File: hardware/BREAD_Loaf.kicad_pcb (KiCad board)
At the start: 2 copper layers, 35.8 x 50.9 mm, 29 parts, among them J1 PPPC101LGBN-RC, J2 THING_PLUS_LOGICAL, Q1 BSS138, Q2 BSS138, Q3 BSS138, U1 AP63205WU-7, U2 LTC4311ISC6-TRMPBF

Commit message: fix(hw): re-point stale library nicknames
These parts exist in KiCad-Master-Lib; the boards referenced libraries that no
longer exist (kml-custom, KML-Custom, and SparkFun libraries that never
contained the part) or names the library has since changed.

KiCad embeds footprint geometry in the .kicad_pcb, so the boards rendered and
fabricated correctly and the rot stayed invisible -- it only surfaces on
update-from-library, or when a generator tries to resolve a nickname.

Nickname/name only. No geometry is changed:

  KML-Custom:Thermal Pad -> KMLib_Mounting:Thermal_Pad
  SparkFun-DiscreteSemi:AP63205 -> KMLib_IC_Power:AP63205WU-7_Buck_Regulator
  SparkFun-LED:WS2812-5050-4PIN -> KMLib_IC_SMD:WS2812-5050-4PIN

Only references that failed to resolve were touched. Generic parts (<=4 pins)
and KiCad *-rescue libraries are deliberately excluded: fingerprint matching
cannot distinguish a 2-pin resistor from a 2-pin capacitor, so those are being
done by hand.
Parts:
- D1: footprint SparkFun-LED:WS2812-5050-4PIN -> KMLib_IC_SMD:WS2812-5050-4PIN
- HS1: footprint KML-Custom:Thermal Pad -> KMLib_Mounting:Thermal_Pad
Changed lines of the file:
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@@
 		(embedded_fonts no)
 	)
-	(footprint "KML-Custom:Thermal Pad"
+	(footprint "KMLib_Mounting:Thermal_Pad"
 		(layer "F.Cu")
 		(at 64.55 112.35)
@@
 		(embedded_fonts no)
 	)
-	(footprint "SparkFun-LED:WS2812-5050-4PIN"
+	(footprint "KMLib_IC_SMD:WS2812-5050-4PIN"
 		(layer "F.Cu")
 		(at 64 121.05 180)

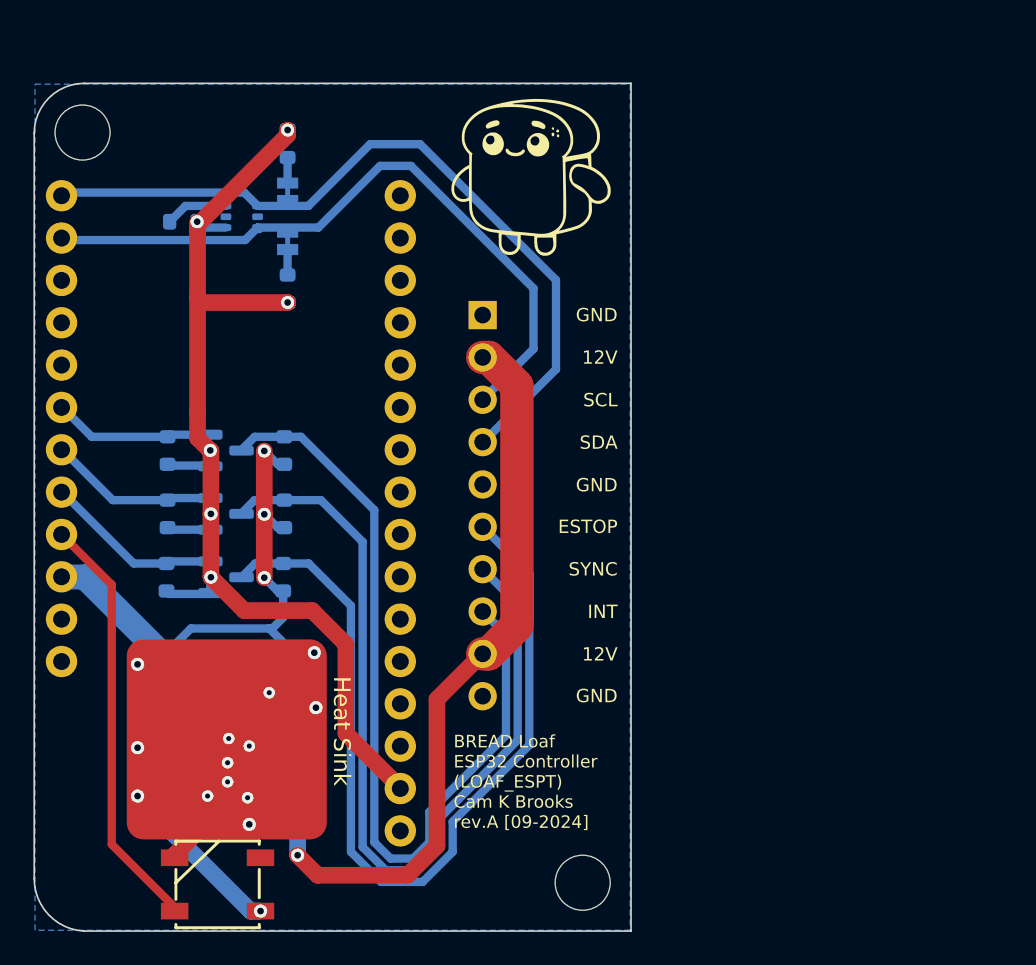
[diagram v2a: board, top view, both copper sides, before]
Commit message: fix(hw): re-point remaining library references
Every symbol now resolves against KiCad-Master-Lib:

  LTC4311:LTC4311ISC6-TRMPBF        -> KMLib_IC_Digital:LTC4311ISC6-TRMPBF
  SparkFun-RF:ESP_THING_PLUS_LOGICAL -> SparkFun-Board:ThingPlus_With_Connectors
  SparkFun-Hardware:Stand_off, PPPC101LGBN-RC, Arc  -> resolved

Board is clean: validate_board PASS, 0 ERC errors, 0 DRC errors.
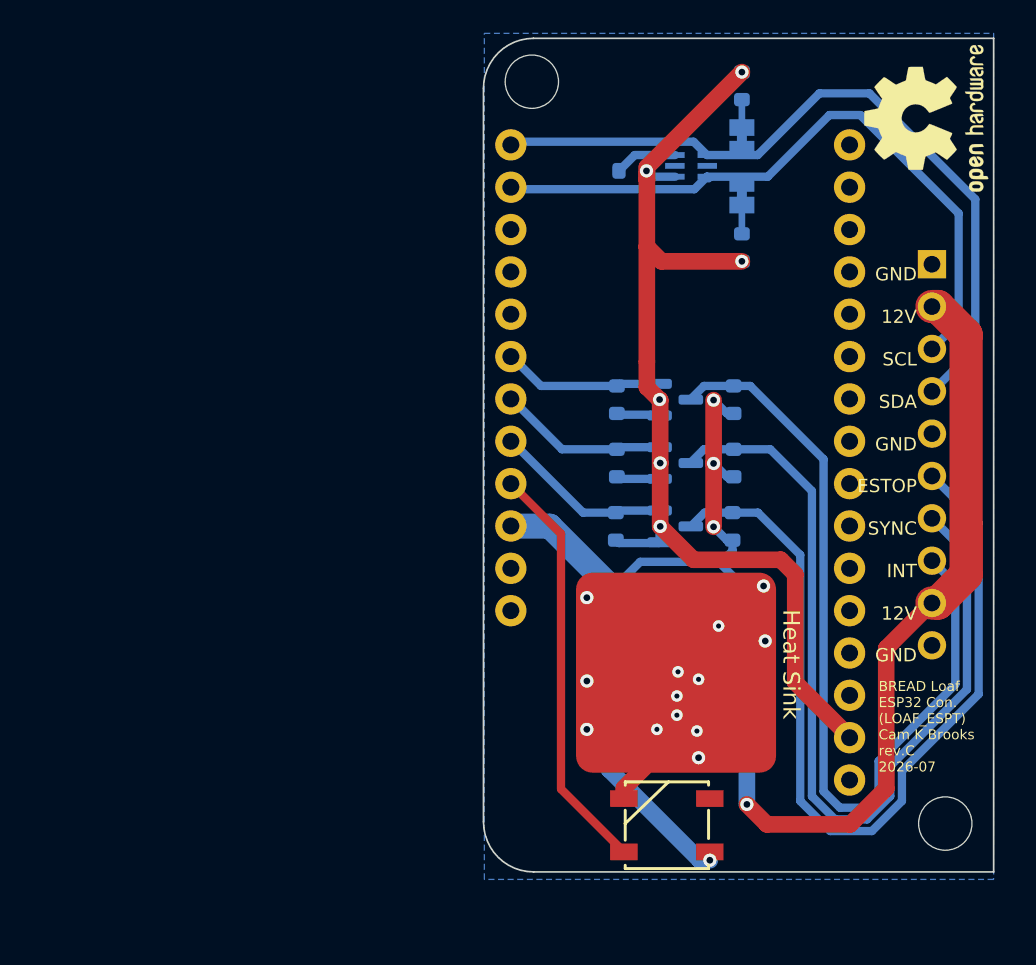
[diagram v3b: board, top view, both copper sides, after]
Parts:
- removed J1: PPPC101LGBN-RC, Connector_PinSocket_2.54mm:PinSocket_1x10_P2.54mm_Horizontal
- removed J2: THING_PLUS_LOGICAL, SparkFun-Board:ThingPlus
- removed JP1, JP2: ~, SparkFun-Jumper:Jumper_2_NC_Trace
- removed ST1, ST2: Stand_off, SparkFun-Hardware:Standoff
- removed demo**: Arc, Arc
- added H1: MountingHole, MountingHole:MountingHole_3.2mm_M3, F.Cu at (107.7, 117.4)
- added H2: MountingHole, MountingHole:MountingHole_3.2mm_M3, F.Cu at (82.8, 72.9)
- added J3: Conn_01x10_Socket, Connector_PinSocket_2.54mm:PinSocket_1x10_P2.54mm_Horizontal, B.Cu at (106.8, 83.8)
- added JP3: SolderJumper_2_Bridged, Jumper:SolderJumper-2_P1.3mm_Bridged_Pad1.0x1.5mm, B.Cu at (95.5, 76.3)
- added JP4: SolderJumper_2_Bridged, Jumper:SolderJumper-2_P1.3mm_Bridged_Pad1.0x1.5mm, B.Cu at (95.5, 79.7)
- added U3: ThingPlus, SparkFun-Board:ThingPlus_With_Connectors, F.Cu at (91.8, 99.5)
- REF**: moved to F.Cu
- U1: footprint Package_TO_SOT_SMD:TSOT-23-6 -> KMLib_IC_SMD:SOIC_05WU-7_DIO
- U2: footprint Package_TO_SOT_SMD:SOT-363_SC-70-6 -> KMLib_IC_SMD:SOT-6_SC_LIT
- moved R8 27.5 mm to (95.5, 73.2)
- moved R9 27.4 mm to (95.5, 82.8)
- moved C1 27.2 mm to (94.2, 110.3)
- moved C2 27.2 mm to (91.7, 103.5)
- moved C3 27.2 mm to (89.0, 110.3)
- moved C4 27.2 mm to (89.0, 113.2)
- moved HS1 27.2 mm to (91.5, 108.3)
- moved L1 27.2 mm to (89.0, 107.0)
- moved U1 27.2 mm to (94.0, 107.0)
- moved D1 27.2 mm to (91.0, 117.5)
- moved Q1 27.1 mm to (91.5, 99.6)
- moved Q2 27.1 mm to (91.5, 95.8)
- moved Q3 27.1 mm to (91.5, 92.0)
- moved R1 27.1 mm to (87.9, 99.6)
- moved R2 27.1 mm to (88.0, 95.8)
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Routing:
- net +3.3V: track 67.4 -> 69.6 mm
- net /SDA_3.3V: track 46.5 -> 45.0 mm
- net /SCL_3.3V: track 41.3 -> 40.1 mm
- net +12V: track 50.6 -> 51.4 mm
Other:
- board size 35.8 x 50.9 mm -> 30.6 x 50 mm
- board text added: "BREAD Loaf ESP32 Con. (LOAF_ESPT) Cam K Brooks rev.C 2026-07"
- board text removed: "BREAD Loaf ESP32 Controller (LOAF_ESPT) Cam K Brooks rev.A [09-2024]"
